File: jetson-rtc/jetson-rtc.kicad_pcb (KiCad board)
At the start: 2 copper layers, 13 x 52 mm, 11 parts, among them J1 Conn_01x04, J2 Conn_02x20_Odd_Even, SW1 SW_Push, U1 DS3231MZ

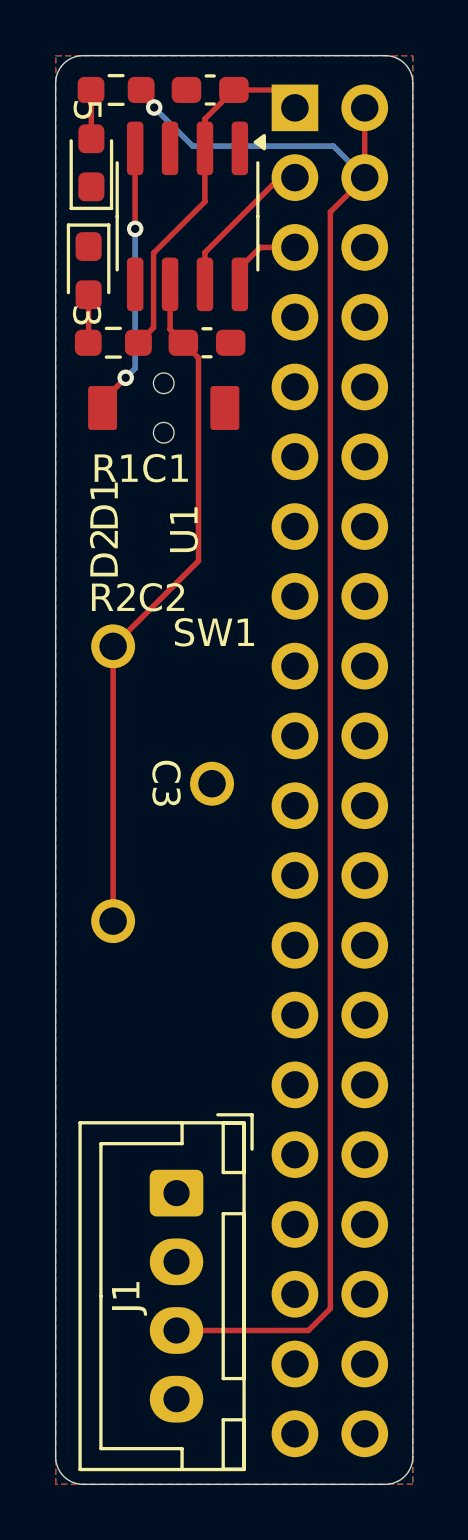
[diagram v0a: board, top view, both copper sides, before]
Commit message: ビア打ち、シルク、ガーバ生成
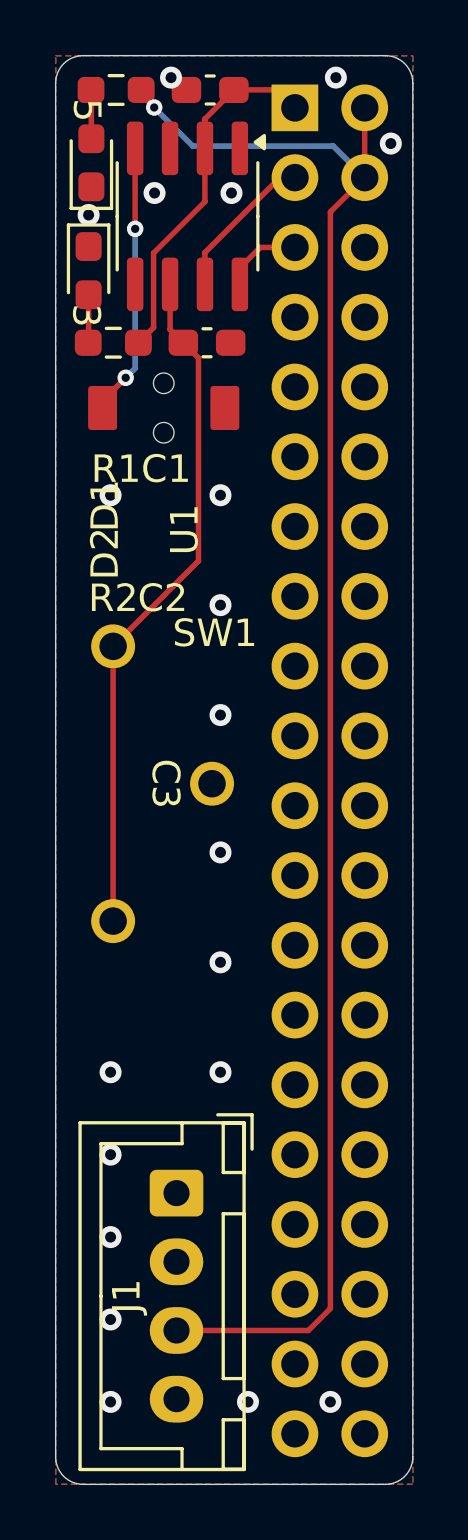
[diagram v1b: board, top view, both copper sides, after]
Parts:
- added G***: LOGO, LOGO, B.Cu at (18.4, 51.0)
- C3: value C_Polarized_US -> CR2032
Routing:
- net GNDD: vias 0 -> 20
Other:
- board text added: "create by ikeda"
- board text added: "jetson-rtc version1.0"
